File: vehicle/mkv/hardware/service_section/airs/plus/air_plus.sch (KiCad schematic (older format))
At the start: 10 parts, among them J1 UF_4_VT, J2 MicroFit_RA_06, J3 MicroFit_RA_4, J4 redcude_7461166, J5 redcude_7461166, K1 DBR71210(NC)

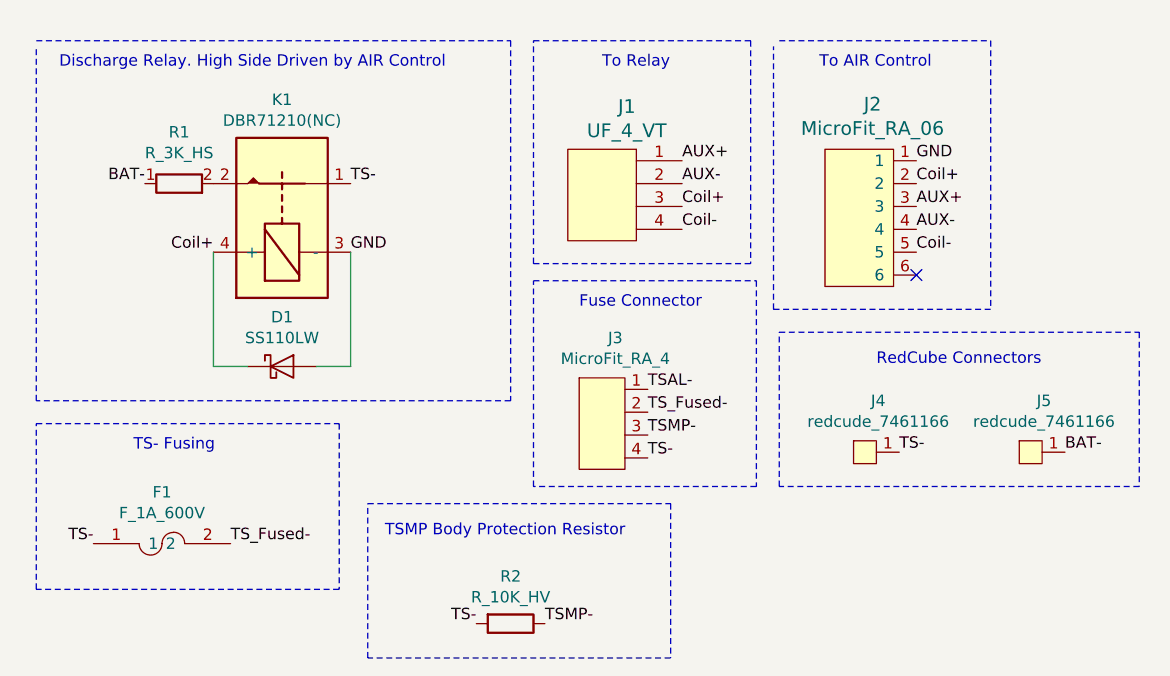
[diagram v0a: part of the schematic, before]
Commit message: fix: make AIR+ and AIR- boards rules compliant (#74)
* fix: adjust routing to provide proper TS/GLVS separation of 4mm

fix: reposition components to fix issues with parts on both sides

fix: adjust sizing of relay model

feat: add footprint for resistor

* fix: move dimension to be visible

* fix: add BUILD files for Bazel

* fix: remove rescue libraries

* fix: correct format for BUILD files
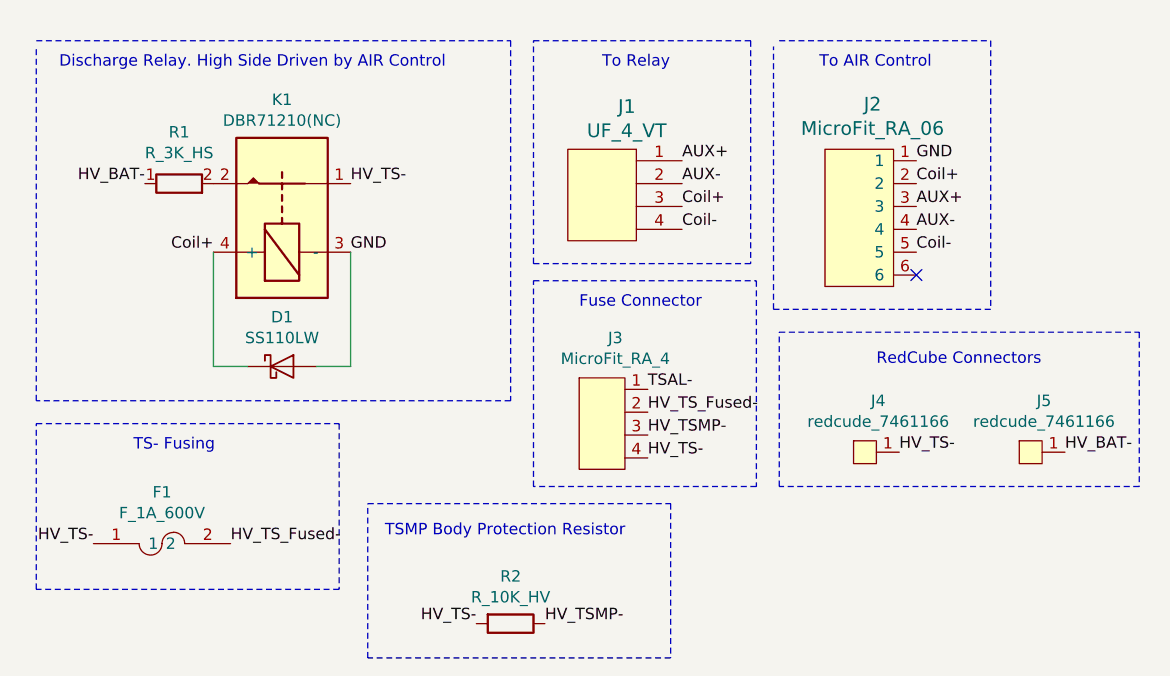
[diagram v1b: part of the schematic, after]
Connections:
- net BAT- renamed HV_BAT-
- net TS- renamed HV_TS-
- net TSMP- renamed HV_TSMP-
- net TS_Fused- renamed HV_TS_Fused-
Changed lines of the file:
@@
 	1750 2325 1600 2325
 Text Label 1075 3100 2    50   ~ 0
-TS-
+HV_TS-
 $Comp
 L Formula:UF_4_VT J1
@@
 $EndComp
 Text Label 4600 2700 0    50   ~ 0
-TS-
+HV_TS-
 $Comp
 L Formula:redcude_7461166 J5
@@
 $EndComp
 Text Label 5325 2700 0    50   ~ 0
-BAT-
+HV_BAT-
 Wire Wire Line
 	1600 1825 1600 2325
@@
 $EndComp
 Text Label 1300 1525 2    50   ~ 0
-BAT-
+HV_BAT-
 Text Label 2200 1525 0    50   ~ 0
-TS-
+HV_TS-
 Wire Wire Line
 	2200 1825 2200 2325
@@
 AUX+
 Text Label 3050 3450 0    50   ~ 0
-TSMP-
+HV_TSMP-
 Text Label 3650 1625 0    50   ~ 0
 Coil+
 Text Label 3500 2725 0    50   ~ 0
-TS-
+HV_TS-
 Text Label 3500 2625 0    50   ~ 0
-TSMP-
+HV_TSMP-
 Text Label 3500 2425 0    50   ~ 0
 TSAL-
@@
 $EndComp
 Text Label 3500 2525 0    50   ~ 0
-TS_Fused-
+HV_TS_Fused-
 NoConn ~ 4675 1925
 Text Label 4675 1525 0    50   ~ 0
@@
 AUX+
 Text Label 1675 3100 0    50   ~ 0
-TS_Fused-
+HV_TS_Fused-
 Text Notes 2000 625  0    50   ~ 0
 NEW AIR PLUS\n
@@
 $EndComp
 Text Label 2750 3450 2    50   ~ 0
-TS-
+HV_TS-
 Wire Notes Line
 	4075 2175 5650 2175

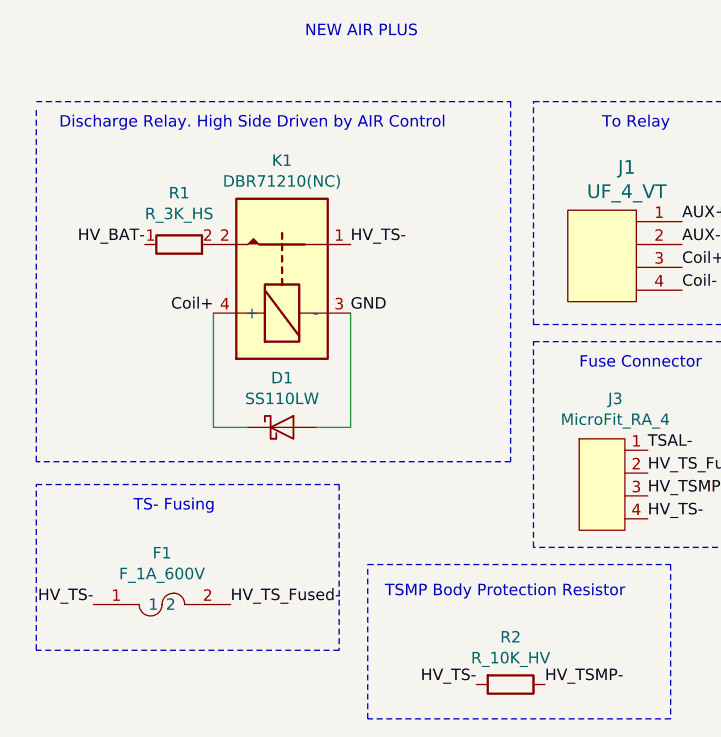
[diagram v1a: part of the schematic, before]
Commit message: feat: redesign air mounts for no conformal coat and 200W relays
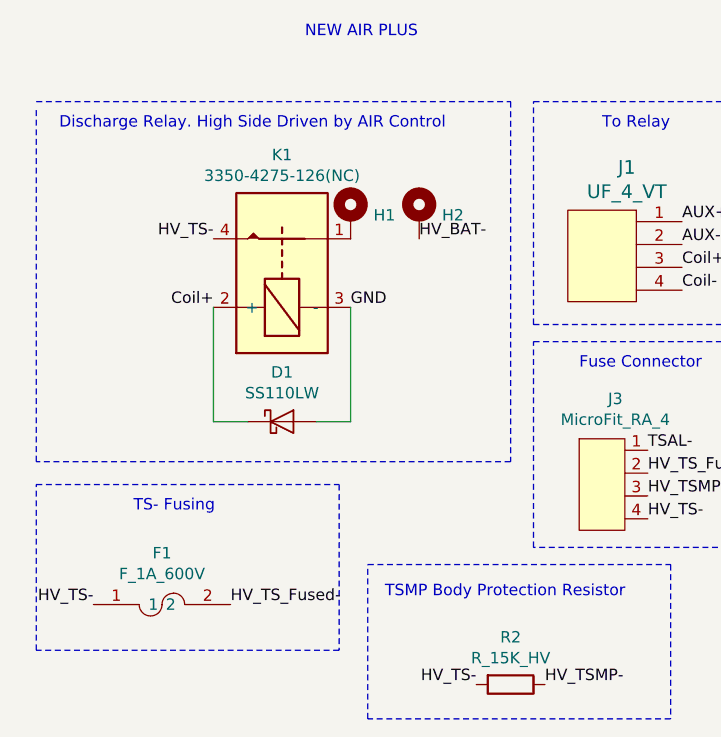
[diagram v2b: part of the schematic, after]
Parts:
- removed K1: DBR71210(NC), footprints:D-Series_Cynergy_Relay, symbol Formula:DBR71210(NC)
- removed R1: R_3K_HS, footprints:R_3k_HS_TO247, symbol Formula:R_3K_HS
- removed R2: R_10K_HV, footprints:R_TSMP_SMD_5329, symbol Formula:R_10K_HV
- added H1, H2: MountingHole_Pad, MountingHole:MountingHole_2.5mm_Pad, symbol Mechanical:MountingHole_Pad
- added K1: 3350-4275-126(NC), footprints:Relay_Comus_3350, symbol formula:3350-4275-126(NC)
- added R2: R_15K_HV, footprints:R_TSMP_SMD_5329, symbol formula:R_15K_HV
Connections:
- net Coil+: now also K1.2 (+)
- net GND: now also K1.3 (-)
- net HV_BAT-: now also H2.1
- net HV_TS-: now also K1.4, R2.2
- net HV_TSMP-: now also R2.1
- new net: H1.1, K1.1
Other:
- moved on the sheet: D1
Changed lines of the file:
@@
 L Formula:SS110LW D1
 U 1 1 5DAE7FAE
-P 1900 2325
-F 0 "D1" H 1900 2541 50  0000 C CNN
-F 1 "SS110LW" H 1900 2450 50  0000 C CNN
-F 2 "footprints:D_SOD-123W_OEM" H 1800 2325 50  0001 C CNN
-F 3 "http://www.taiwansemi.com/products/datasheet/SS14LW%20SERIES_A1511.pdf" H 1900 2425 50  0001 C CNN
-F 4 "DK" H 2100 2625 60  0001 C CNN "MFN"
-F 5 "SS110LWRVGCT-ND" H 2000 2525 60  0001 C CNN "MPN"
-F 6 "https://www.digikey.com/product-detail/en/taiwan-semiconductor-corporation/SS110LW-RVG/SS110LWRVGCT-ND/7359346" H 2200 2725 60  0001 C CNN "PurchasingLink"
-	1    1900 2325
-	1    0    0    -1
-$EndComp
-Wire Wire Line
-	2200 2325 2050 2325
-Wire Wire Line
-	1750 2325 1600 2325
+P 1900 2300
+F 0 "D1" H 1900 2516 50  0000 C CNN
+F 1 "SS110LW" H 1900 2425 50  0000 C CNN
+F 2 "footprints:D_SOD-123W_OEM" H 1800 2300 50  0001 C CNN
+F 3 "http://www.taiwansemi.com/products/datasheet/SS14LW%20SERIES_A1511.pdf" H 1900 2400 50  0001 C CNN
+F 4 "DK" H 2100 2600 60  0001 C CNN "MFN"
+F 5 "SS110LWRVGCT-ND" H 2000 2500 60  0001 C CNN "MPN"
+F 6 "https://www.digikey.com/product-detail/en/taiwan-semiconductor-corporation/SS110LW-RVG/SS110LWRVGCT-ND/7359346" H 2200 2700 60  0001 C CNN "PurchasingLink"
+	1    1900 2300
+	1    0    0    -1
+$EndComp
 Text Label 1075 3100 2    50   ~ 0
 HV_TS-
@@
 Text Label 5325 2700 0    50   ~ 0
 HV_BAT-
-Wire Wire Line
-	1600 1825 1600 2325
 $Comp
 L Formula:F_1A_600V F1
@@
 	1    0    0    -1
 $EndComp
-$Comp
-L Formula:R_3K_HS R1
-U 1 1 5E59D5EA
-P 1450 1525
-F 0 "R1" V 1675 1525 50  0000 C CNN
-F 1 "R_3K_HS" V 1584 1525 50  0000 C CNN
-F 2 "footprints:R_3k_HS_TO247" H 1380 1525 50  0001 C CNN
-F 3 "http://dpk3n3gg92jwt.cloudfront.net/domains/ohmite/pdf/acl_ap101.pdf" H 1530 1525 50  0001 C CNN
-F 4 "DK" H 1450 1525 60  0001 C CNN "MFN"
-F 5 "AP1013KJ-ND" H 1450 1525 60  0001 C CNN "MPN"
-F 6 "https://www.digikey.com/product-detail/en/ohmite/AP101-3K-J/AP101-3K-J-ND/5878525" H 1930 1925 60  0001 C CNN "PurchasingLink"
-F 7 "345-1223-ND" V 2030 2025 60  0001 C CNN "MPN2"
-F 8 "https://www.digikey.com/product-detail/en/wakefield-vette/657-15ABPEN/345-1223-ND/3945700" V 2130 2125 60  0001 C CNN "PurchasingLink2"
-	1    1450 1525
-	0    -1   -1   0
-$EndComp
-Text Label 1300 1525 2    50   ~ 0
+Text Label 2500 1500 0    50   ~ 0
 HV_BAT-
-Text Label 2200 1525 0    50   ~ 0
-HV_TS-
-Wire Wire Line
-	2200 1825 2200 2325
-Text Label 2200 1825 0    50   ~ 0
+Text Label 1600 1500 2    50   ~ 0
+HV_TS-
+Text Label 2200 1800 0    50   ~ 0
 GND
-Text Label 1600 1825 2    50   ~ 0
+Text Label 1600 1800 2    50   ~ 0
 Coil+
 Text Label 3650 1525 0    50   ~ 0
@@
 Text Notes 2000 625  0    50   ~ 0
 NEW AIR PLUS\n
-$Comp
-L Formula:DBR71210(NC) K1
-U 1 1 5E5D8E84
-P 1900 1625
-F 0 "K1" V 2367 1625 50  0000 C CNN
-F 1 "DBR71210(NC)" V 2276 1625 50  0000 C CNN
-F 2 "footprints:D-Series_Cynergy_Relay" H 2350 1575 50  0001 L CNN
-F 3 "https://www.cynergy3.com/sites/default/files/D%20series%202016_5.pdf" H 2350 1275 50  0001 L CNN
-F 4 "DK" H 2750 2175 60  0001 C CNN "MFN"
-F 5 "725-1049-ND" H 2650 2075 60  0001 C CNN "MPN"
-F 6 "https://www.digikey.com/product-detail/en/cynergy-3/DBR71210/725-1049-ND/752025" H 2850 2275 60  0001 C CNN "PurchasingLink"
-	1    1900 1625
-	0    -1   -1   0
-$EndComp
 Text Notes 925  1025 0    50   ~ 0
 Discharge Relay. High Side Driven by AIR Control
@@
 Wire Notes Line
 	2275 3600 2275 2925
-$Comp
-L Formula:R_10K_HV R2
-U 1 1 5E57A605
+Text Label 2750 3450 2    50   ~ 0
+HV_TS-
+Wire Notes Line
+	4075 2175 5650 2175
+Wire Notes Line
+	5650 2175 5650 2850
+Wire Notes Line
+	5650 2850 4075 2850
+Wire Notes Line
+	4075 2850 4075 2175
+$Comp
+L formula:3350-4275-126(NC) K1
+U 1 1 6258A753
+P 1900 1600
+F 0 "K1" V 2367 1600 50  0000 C CNN
+F 1 "3350-4275-126(NC)" V 2276 1600 50  0000 C CNN
+F 2 "footprints:Relay_Comus_3350" H 2350 1550 50  0001 L CNN
+F 3 "https://www.comus-intl.com/wp-content/uploads/2017/01/High-Voltage-Reed-Relays.pdf" H 2350 1250 50  0001 L CNN
+F 4 "DK" H 2750 2150 60  0001 C CNN "MFN"
+F 5 "3350-4275-126" H 2650 2050 60  0001 C CNN "MPN"
+F 6 "https://www.digikey.com/en/products/detail/comus-international/3350-4275-126/7515922" H 2850 2250 60  0001 C CNN "PurchasingLink"
+	1    1900 1600
+	0    -1   -1   0
+$EndComp
+Wire Wire Line
+	1750 2300 1600 2300
+Wire Wire Line
+	1600 2300 1600 1800
+Wire Wire Line
+	2050 2300 2200 2300
+Wire Wire Line
+	2200 2300 2200 1800
+$Comp
+L formula:R_15K_HV R2
+U 1 1 625A23A2
 P 2900 3450
 F 0 "R2" V 2693 3450 50  0000 C CNN
-F 1 "R_10K_HV" V 2784 3450 50  0000 C CNN
+F 1 "R_15K_HV" V 2784 3450 50  0000 C CNN
 F 2 "footprints:R_TSMP_SMD_5329" H 2830 3450 50  0001 C CNN
-F 3 "http://www.vishay.com/docs/28731/pacserie.pdf" H 2980 3450 50  0001 C CNN
+F 3 "https://www.te.com/commerce/DocumentDelivery/DDEController?Action=srchrtrv&DocNm=1773242&DocType=DS&DocLang=English" H 2980 3450 50  0001 C CNN
 F 4 "DK" H 2900 3450 60  0001 C CNN "MFN"
-F 5 "PPC5D10.0KCT-ND " H 2900 3450 60  0001 C CNN "MPN"
-F 6 "https://www.digikey.com/products/en?keywords=PPC5D10.0KCT-ND" H 3380 3850 60  0001 C CNN "PurchasingLink"
+F 5 "SMF515KJT" H 2900 3450 60  0001 C CNN "MPN"
+F 6 "https://www.digikey.com/en/products/detail/te-connectivity-passive-product/SMF515KJT/2367113" H 3380 3850 60  0001 C CNN "PurchasingLink"
 	1    2900 3450
 	0    1    1    0
 $EndComp
-Text Label 2750 3450 2    50   ~ 0
-HV_TS-
-Wire Notes Line
-	4075 2175 5650 2175
-Wire Notes Line
-	5650 2175 5650 2850
-Wire Notes Line
-	5650 2850 4075 2850
-Wire Notes Line
-	4075 2850 4075 2175
+$Comp
+L Mechanical:MountingHole_Pad H1
+U 1 1 62595E8A
+P 2200 1400
+F 0 "H1" H 2300 1403 50  0000 L CNN
+F 1 "MountingHole_Pad" H 2300 1358 50  0001 L CNN
+F 2 "MountingHole:MountingHole_2.5mm_Pad" H 2200 1400 50  0001 C CNN
+F 3 "~" H 2200 1400 50  0001 C CNN
+	1    2200 1400
+	1    0    0    -1
+$EndComp
+$Comp
+L Mechanical:MountingHole_Pad H2
+U 1 1 6259B2C1
+P 2500 1400
+F 0 "H2" H 2600 1403 50  0000 L CNN
+F 1 "MountingHole_Pad" H 2600 1358 50  0001 L CNN
+F 2 "MountingHole:MountingHole_2.5mm_Pad" H 2500 1400 50  0001 C CNN
+F 3 "~" H 2500 1400 50  0001 C CNN
+	1    2500 1400
+	1    0    0    -1
+$EndComp
 $EndSCHEMATC

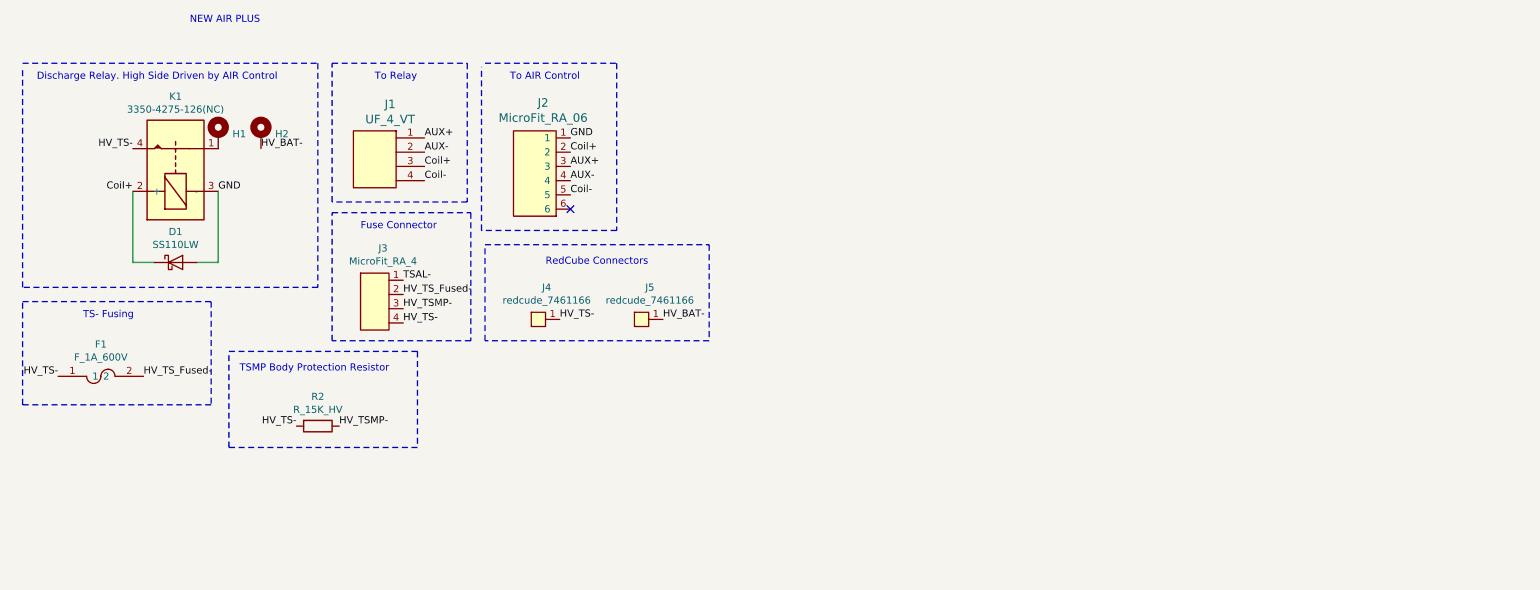
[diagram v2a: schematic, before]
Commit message: fix: modify discharge circuit to connect to correct busbar
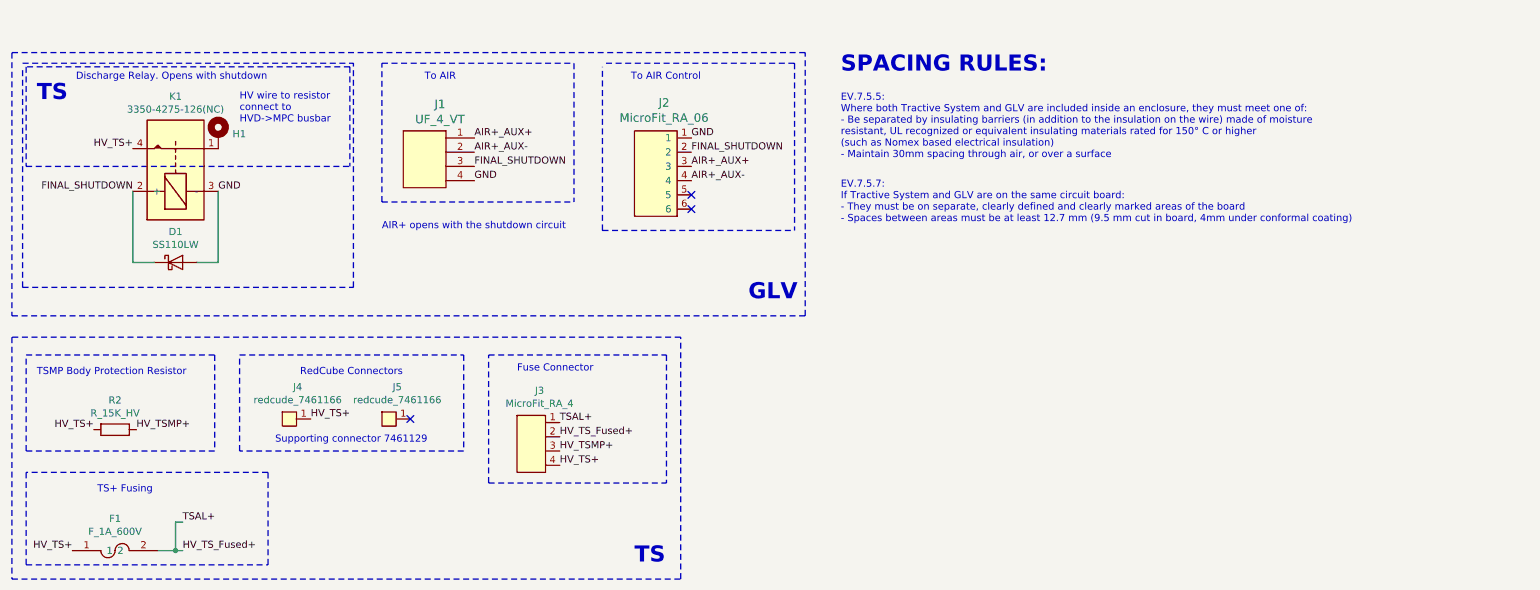
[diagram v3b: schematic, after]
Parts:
- removed H2: MountingHole_Pad, MountingHole:MountingHole_2.5mm_Pad, symbol Mechanical:MountingHole_Pad
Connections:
- net TSAL- is gone; now on net HV_TS_Fused+: J3.1
- net GND: now also J1.4
- net AUX+ renamed AIR+_AUX+
- net AUX- renamed AIR+_AUX-
- net Coil+ renamed FINAL_SHUTDOWN
- net Coil-: no longer names the net of J2.5
- net Coil-: no longer J1.4
- net HV_BAT-: no longer names the net of J5.1
- net HV_TS- renamed HV_TS+
- net HV_TSMP- renamed HV_TSMP+
- net HV_TS_Fused- renamed HV_TS_Fused+
- no-connect marks 1 -> 3
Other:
- note added: "AIR+ opens with the shutdown circuit"
- note added: "Discharge Relay. Opens with shutdown"
- note added: "EV.7.5.5:\nWhere both Tractive System and GLV are included inside an enclosure, they must meet one of:\n- Be separated by insulating barriers (in addition to the insulation on the wire) made of moisture\nresistant, UL recognized or equivalent insulating materials rated for 150° C or higher \n(such as Nomex based electrical insulation)\n- Maintain 30mm spacing through air, or over a surface"
- note added: "EV.7.5.7:\nIf Tractive System and GLV are on the same circuit board: \n- They must be on separate, clearly defined and clearly marked areas of the board\n- Spaces between areas must be at least 12.7 mm (9.5 mm cut in board, 4mm under conformal coating)"
- note added: "GLV"
- note added: "HV wire to resistor\nconnect to \nHVD->MPC busbar"
- note added: "SPACING RULES:"
- note added: "Supporting connector 7461129"
- note added: "TS"
- note added: "TS+ Fusing"
- note added: "To AIR\n"
- note removed: "Discharge Relay. High Side Driven by AIR Control"
- note removed: "NEW AIR PLUS\n"
- note removed: "TS- Fusing"
- note removed: "To Relay\n"
- moved on the sheet: F1, J1, J2, J3, J4, J5, R2

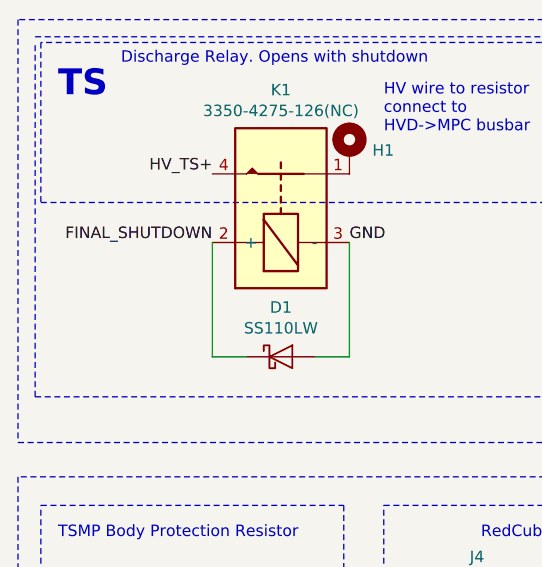
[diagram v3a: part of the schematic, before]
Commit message: fix: add resistor to limit relay voltage to operating range
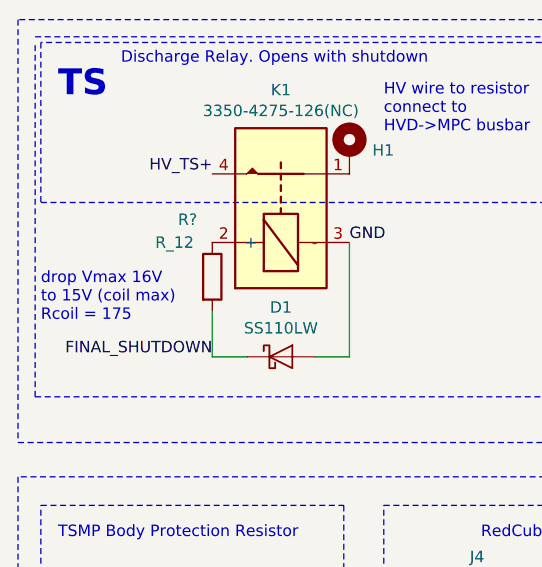
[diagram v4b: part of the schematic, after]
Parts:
- added R?: R_12, footprints:R_0805_OEM, symbol formula:R_12
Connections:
- net FINAL_SHUTDOWN: now also R?.2; no longer K1.2 (+)
- new net: K1.2 (+), R?.1
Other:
- note added: "drop Vmax 16V \nto 15V (coil max)\nRcoil = 175"
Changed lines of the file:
@@
 Text Label 2200 1800 0    50   ~ 0
 GND
-Text Label 1600 1800 2    50   ~ 0
+Text Label 1600 2300 2    50   ~ 0
 FINAL_SHUTDOWN
 Text Label 4000 1525 0    50   ~ 0
@@
 	1750 2300 1600 2300
 Wire Wire Line
-	1600 2300 1600 1800
-Wire Wire Line
 	2050 2300 2200 2300
 Wire Wire Line
@@
 SPACING RULES:
 NoConn ~ 3550 3400
+Text Notes 850  2150 0    50   ~ 0
+drop Vmax 16V \nto 15V (coil max)\nRcoil = 175
+$Comp
+L formula:R_12 R?
+U 1 1 6262A6E0
+P 1600 1950
+F 0 "R?" H 1450 2200 50  0000 L CNN
+F 1 "R_12" H 1350 2100 50  0000 L CNN
+F 2 "footprints:R_0805_OEM" V 1530 1950 50  0001 C CNN
+F 3 "https://www.te.com/commerce/DocumentDelivery/DDEController?Action=srchrtrv&DocNm=1773200-1&DocType=DS&DocLang=English" V 1680 1950 50  0001 C CNN
+F 4 "TE" V 1780 2050 60  0001 C CNN "MFN"
+F 5 "CPF-A-0805B12RE" V 1880 2150 60  0001 C CNN "MPN"
+F 6 "https://www.digikey.com/en/products/detail/te-connectivity-passive-product/CPF-A-0805B12RE/5583863" V 1880 2150 60  0001 C CNN "PurchasingLink"
+	1    1600 1950
+	1    0    0    -1
+$EndComp
+Wire Wire Line
+	1600 2100 1600 2300
 $EndSCHEMATC
